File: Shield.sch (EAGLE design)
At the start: 1 part

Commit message: More to do listing
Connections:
- new net ESC_SIG1: B1.9
- new net ESC_SIG2: B1.10
- new net ESC_SIG3: B1.11
- new net ESC_SIG4: B1.6
- new net ESC_SIG5: B1.5
- new net ESC_SIG6: B1.3
- new net PWM1: B1.7
- new net PWM2: B1.8
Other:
- note added: "Capacitors (multiple sizes)"
- note added: "Don't forget labels :)"
- note added: "Optional flyback diodes"
- note added: "Power LEDs"
- note added: "Reverse voltage protection"
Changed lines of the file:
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@@
 <text x="43.18" y="83.82" size="1.778" layer="91">ESC solder bridges or header connections</text>
 <text x="182.88" y="22.86" size="1.778" layer="91">https://www.arduino.cc/en/uploads/Main/arduino-mega2560-schematic.pdf</text>
+<text x="15.24" y="93.98" size="1.778" layer="91">Capacitors (multiple sizes)</text>
+<text x="15.24" y="91.44" size="1.778" layer="91">Optional flyback diodes</text>
+<text x="33.02" y="170.18" size="1.778" layer="91">Reverse voltage protection</text>
+<text x="76.2" y="144.78" size="1.27" layer="91">Power LEDs</text>
+<text x="289.56" y="66.04" size="1.27" layer="91">Don't forget labels :)</text>
 </plain>
 <instances>
@@
 </segment>
 </net>
+<net name="ESC_SIG1" class="0">
+<segment>
+<pinref part="B1" gate="G$1" pin="9"/>
+<wire x1="203.2" y1="60.96" x2="200.66" y2="60.96" width="0.1524" layer="91"/>
+<label x="200.66" y="60.96" size="1.27" layer="95" rot="R180" xref="yes"/>
+</segment>
+</net>
+<net name="ESC_SIG2" class="0">
+<segment>
+<pinref part="B1" gate="G$1" pin="10"/>
+<wire x1="203.2" y1="58.42" x2="200.66" y2="58.42" width="0.1524" layer="91"/>
+<label x="200.66" y="58.42" size="1.27" layer="95" rot="R180" xref="yes"/>
+</segment>
+</net>
+<net name="ESC_SIG3" class="0">
+<segment>
+<pinref part="B1" gate="G$1" pin="11"/>
+<wire x1="203.2" y1="55.88" x2="200.66" y2="55.88" width="0.1524" layer="91"/>
+<label x="200.66" y="55.88" size="1.27" layer="95" rot="R180" xref="yes"/>
+</segment>
+</net>
+<net name="ESC_SIG4" class="0">
+<segment>
+<pinref part="B1" gate="G$1" pin="6"/>
+<wire x1="203.2" y1="68.58" x2="200.66" y2="68.58" width="0.1524" layer="91"/>
+<label x="200.66" y="68.58" size="1.27" layer="95" rot="R180" xref="yes"/>
+</segment>
+</net>
+<net name="ESC_SIG5" class="0">
+<segment>
+<pinref part="B1" gate="G$1" pin="5"/>
+<wire x1="203.2" y1="71.12" x2="200.66" y2="71.12" width="0.1524" layer="91"/>
+<label x="200.66" y="71.12" size="1.27" layer="95" rot="R180" xref="yes"/>
+</segment>
+</net>
+<net name="ESC_SIG6" class="0">
+<segment>
+<pinref part="B1" gate="G$1" pin="3"/>
+<wire x1="203.2" y1="76.2" x2="200.66" y2="76.2" width="0.1524" layer="91"/>
+<label x="200.66" y="76.2" size="1.27" layer="95" rot="R180" xref="yes"/>
+</segment>
+</net>
+<net name="PWM1" class="0">
+<segment>
+<pinref part="B1" gate="G$1" pin="7"/>
+<wire x1="203.2" y1="66.04" x2="200.66" y2="66.04" width="0.1524" layer="91"/>
+<label x="200.66" y="66.04" size="1.27" layer="95" rot="R180" xref="yes"/>
+</segment>
+</net>
+<net name="PWM2" class="0">
+<segment>
+<pinref part="B1" gate="G$1" pin="8"/>
+<wire x1="203.2" y1="63.5" x2="200.66" y2="63.5" width="0.1524" layer="91"/>
+<label x="200.66" y="63.5" size="1.27" layer="95" rot="R180" xref="yes"/>
+</segment>
+</net>

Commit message: Split into two sheets and add most existing parts
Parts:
- added C1: 1mF, SparkFun-Capacitors:1000UF-RADIAL-5MM-25V-20%
- added C2: 100uF, SparkFun-Capacitors:100UF-POLAR-RADIAL-2.5MM-25V-20%
- added D1, D2: (no value), SparkFun-LED:LED3MM
- added D3: (no value), diode:SCHOTTKY-DIODECB429-15
- added J1, J12, J13, J14, J15, J17, J18, J2: (no value), SparkFun-Connectors:CONN_02
- added J10, J11: (no value), Banana Plug PTH:BANANA_PTH
- added J16: (no value), SparkFun-Connectors:CONN_03-SCREW-5MM
- added J3, J4, J5: (no value), SparkFun-Connectors:CONN_03
- added J6: (no value), SparkFun-Connectors:CONN_04
- added J7, J8, J9: DF13-4P-1.25DSA, con-hirose-df13:DF13-4P-1.25DSA
- added JP1, JP2: JUMPER-SMT_2_NO_SILK, SparkFun-Jumpers:JUMPER-SMT_2_NO_SILK
- added Q1: 60V/32A/35mΩ, SparkFun-DiscreteSemi:MOSFET-NCH-FQP30N06L
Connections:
- new net 12V: D1.A, D3.A, J1.2, J10.1, J17.2, JP2.1, Q1.G
- new net 3V3: B1.3.3V, J6.4, J7.1, J8.1, J9.1
- new net GND_RAW: J11.1, Q1.D
- new net N$1: J16.3
- new net N$2: J13.1, JP1.1
- new net N$3: J13.2, JP1.2
- new net N$4: C1.+, C2.+, D3.C, JP2.2
- new net N$5: J16.2
- new net N$6: J16.1
- new net PWM3: B1.4, J5.3
- new net SCL: J6.3, J7.2, J8.2, J9.2
- new net SDA: J6.2, J7.3, J8.3, J9.3
- net 5V: now also D2.A, J12.2, J14.2, J15.2, J18.2, J2.2, J3.2, J4.2, J5.2
- net GND: now also C1.-, C2.-, D1.C, D2.C, J1.1, J12.1, J14.1, J15.1, J17.1, J18.1, J2.1, J3.1, J4.1, J5.1, J6.1, J7.4, J8.4, J9.4, Q1.S
- net PWM1: now also J3.3
- net PWM2: now also J4.3
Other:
- note added: "5 mm screw terminal connector"
- note added: "5V outputs (and usb)"
- note added: "Fuses"
- note added: "I2C Breakout & Connectors"
- note added: "Mounting holes"
- note added: "Multiple size capacitors. Pick the value to your application"
- note added: "Optional schottky diode for back emf protection"
- note added: "PWM Connectors"
- note added: "Solder jumper / header jumper for connecting & disconnecting PWM signal"
- note added: "Voltage Testpoints and power indicator LEDs"
- note removed: "5V outputs"
- note removed: "Capacitors (multiple sizes)"
- note removed: "ESC connections"
- note removed: "ESC solder bridges or header connections"
- note removed: "I2C breakouts"
- note removed: "Optional flyback diodes"
- note removed: "Power LEDs"
- note removed: "Servo headers"

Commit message: Finish all parts except fuses
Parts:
- added C10, C12, C4, C6, C8: 100uF, SparkFun-Capacitors:100UF-POLAR-RADIAL-2.5MM-25V-20%
- added C11, C3, C5, C7, C9: 1mF, SparkFun-Capacitors:1000UF-RADIAL-5MM-25V-20%
- added D4, D5, D6, D7, D8: (no value), diode:SCHOTTKY-DIODECB429-15
- added H1, H2, H3, H4, H5, H6: 6-32-HOLE, Mounting Holes:6-32-HOLE
- added J19, J21, J23, J25, J27: (no value), SparkFun-Connectors:CONN_02
- added J20, J22, J24, J26, J28: (no value), SparkFun-Connectors:CONN_03-SCREW-5MM
- added J29: (no value), SparkFun-Connectors:CONN_03
- added J30: (no value), Anderson PP:ANDERON_POWERPOLE_2
- added JP10, JP11, JP12, JP13, JP14, JP15, JP16, JP3, JP4, JP5, JP6, JP7, JP8, JP9: JUMPER-SMT_2_NO_SILK, SparkFun-Jumpers:JUMPER-SMT_2_NO_SILK
- added R1, R2: 10k, SparkFun-Resistors:10KOHM-HORIZ-1/4W-5%
- added U$1, U$2, U$3, U$4, U$5, U$6: ESC, ESC:ESC
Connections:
- removed net N$1: J16.3
- removed net N$2: J13.1, JP1.1
- removed net N$3: J13.2, JP1.2
- removed net N$4: C1.+, C2.+, D3.C, JP2.2
- removed net N$5: J16.2
- removed net N$6: J16.1
- new net 12V_ESC1: C1.+, C2.+, D3.C, JP2.2, U$1.VCC
- new net 12V_ESC2: C3.+, C4.+, D4.C, JP8.2, U$2.VCC
- new net 12V_ESC3: C5.+, C6.+, D5.C, JP10.2, U$3.VCC
- new net 12V_ESC4: C7.+, C8.+, D6.C, JP12.2, U$4.VCC
- new net 12V_ESC5: C10.+, C9.+, D7.C, JP14.2, U$5.VCC
- new net 12V_ESC6: C11.+, C12.+, D8.C, JP16.2, U$6.VCC
- new net ESC1_PH1: J16.3, U$1.RED
- new net ESC1_PH2: J16.2, U$1.YEL
- new net ESC1_PH3: J16.1, U$1.BLK
- new net ESC2_PH1: J20.3, U$2.RED
- new net ESC2_PH2: J20.2, U$2.YEL
- new net ESC2_PH3: J20.1, U$2.BLK
- new net ESC3_PH1: J22.3, U$3.RED
- new net ESC3_PH2: J22.2, U$3.YEL
- new net ESC3_PH3: J22.1, U$3.BLK
- new net ESC4_PH1: J24.3, U$4.RED
- new net ESC4_PH2: J24.2, U$4.YEL
- new net ESC4_PH3: J24.1, U$4.BLK
- new net ESC5_PH1: J26.3, U$5.RED
- new net ESC5_PH2: J26.2, U$5.YEL
- new net ESC5_PH3: J26.1, U$5.BLK
- new net ESC6_PH1: J28.3, U$6.RED
- new net ESC6_PH2: J28.2, U$6.YEL
- new net ESC6_PH3: J28.1, U$6.BLK
- new net ESC_SIG_PIN1: J13.2, JP1.2, U$1.PWM_SGN
- new net ESC_SIG_PIN2: J19.2, JP7.2, U$2.PWM_SGN
- new net ESC_SIG_PIN3: J21.2, JP9.2, U$3.PWM_SGN
- new net ESC_SIG_PIN4: J23.2, JP11.2, U$4.PWM_SGN
- new net ESC_SIG_PIN5: J25.2, JP13.2, U$5.PWM_SGN
- new net ESC_SIG_PIN6: J27.2, JP15.2, U$6.PWM_SGN
- new net N$10: B1.A5, JP4.2
- new net N$7: JP5.1, JP6.1, R1.2, R2.2
- new net N$9: B1.A4, JP3.2
- net 12V: now also D4.A, D5.A, D6.A, D7.A, D8.A, J29.3, J30.POS, JP10.1, JP12.1, JP14.1, JP16.1, JP8.1
- net 3V3: now also JP5.2
- net 5V: now also J29.1, JP6.2
- net ESC_SIG1: now also J13.1, JP1.1
- net ESC_SIG2: now also J19.1, JP7.1
- net ESC_SIG3: now also J21.1, JP9.1
- net ESC_SIG4: now also J23.1, JP11.1
- net ESC_SIG5: now also J25.1, JP13.1
- net ESC_SIG6: now also J27.1, JP15.1
- net GND: now also C10.-, C11.-, C12.-, C3.-, C4.-, C5.-, C6.-, C7.-, C8.-, C9.-, J29.2, U$1.GND, U$1.PWM_GND, U$2.GND, U$2.PWM_GND, U$3.GND, U$3.PWM_GND, U$4.GND, U$4.PWM_GND, U$5.GND, U$5.PWM_GND, U$6.GND, U$6.PWM_GND
- net GND_RAW: now also J30.NEG
- net SCL: now also B1.21(SCL), JP4.1, R1.1
- net SDA: now also B1.20(SDA), JP3.1, R2.1
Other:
- note added: "12->5V converter Use a board mount power supply like CUI P78E-1000 or recom INNOLINE R-78E. Or connect and external one with wires"
- note added: "5V outputs"
- note added: "Populate eiter JP5 or JP6 (not both) for I2C logic level"
- note added: "https://www.arduino.cc/en/uploads/Main/arduino-uno-schematic.pdf https://www.arduino.cc/en/uploads/Main/arduino-mega2560-schematic.pdf"
- note removed: "12->5V converter"
- note removed: "5V outputs (and usb)"
- note removed: "6x ESCs"
- note removed: "https://www.arduino.cc/en/uploads/Main/arduino-mega2560-schematic.pdf"
- moved on the sheet: C1, C2, D3, J12, J13, J14, J15, J16, JP1, JP2

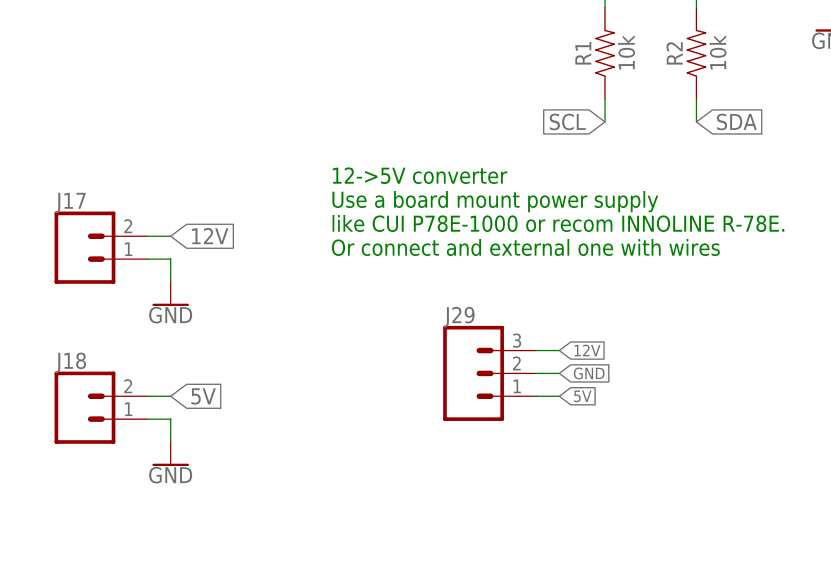
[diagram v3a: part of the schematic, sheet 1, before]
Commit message: Add caps around buck converter (fixes #1)
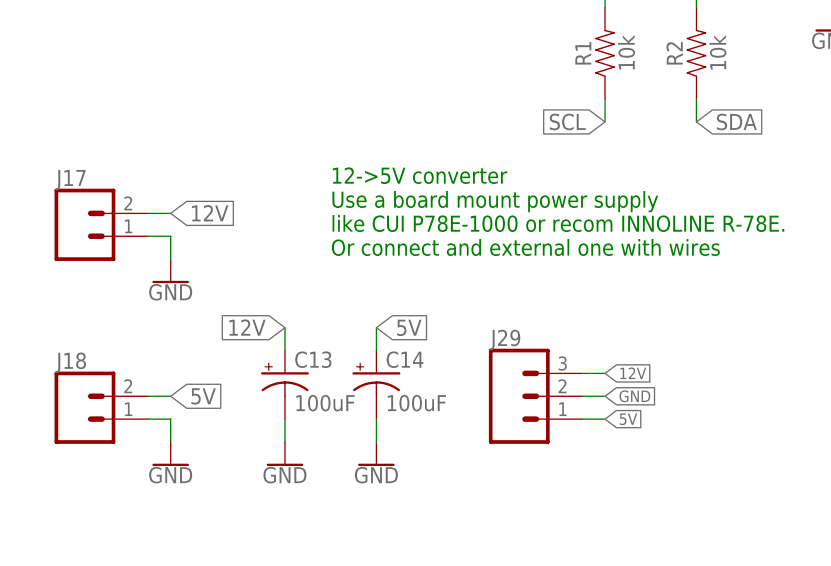
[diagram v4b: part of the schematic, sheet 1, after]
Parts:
- added C13, C14: 100uF, SparkFun-Capacitors:100UF-POLAR-RADIAL-2.5MM-25V-20%
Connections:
- net 12V: now also C13.+
- net 5V: now also C14.+
- net GND: now also C13.-, C14.-
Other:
- moved on the sheet: J17, J29
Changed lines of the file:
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@@
 <part name="J29" library="SparkFun-Connectors" library_urn="urn:adsk.eagle:library:513" deviceset="CONN_03" device="" package3d_urn="urn:adsk.eagle:package:38063/1"/>
 <part name="J30" library="Anderson PP" deviceset="ANDERON_POWERPOLE_2" device=""/>
+<part name="C13" library="SparkFun-Capacitors" library_urn="urn:adsk.eagle:library:510" deviceset="100UF-POLAR" device="-RADIAL-2.5MM-25V-20%" package3d_urn="urn:adsk.eagle:package:37415/1" value="100uF"/>
+<part name="C14" library="SparkFun-Capacitors" library_urn="urn:adsk.eagle:library:510" deviceset="100UF-POLAR" device="-RADIAL-2.5MM-25V-20%" package3d_urn="urn:adsk.eagle:package:37415/1" value="100uF"/>
+<part name="GND31" library="SparkFun-PowerSymbols" library_urn="urn:adsk.eagle:library:530" deviceset="GND" device=""/>
+<part name="GND32" library="SparkFun-PowerSymbols" library_urn="urn:adsk.eagle:library:530" deviceset="GND" device=""/>
 </parts>
 <sheets>
@@
 <attribute name="VALUE" x="33.02" y="68.326" size="1.778" layer="96" align="top-center"/>
 </instance>
-<instance part="J17" gate="G$1" x="7.62" y="33.02" smashed="yes">
-<attribute name="VALUE" x="5.08" y="28.194" size="1.778" layer="96" font="vector"/>
-<attribute name="NAME" x="5.08" y="38.608" size="1.778" layer="95" font="vector"/>
+<instance part="J17" gate="G$1" x="7.62" y="35.56" smashed="yes">
+<attribute name="VALUE" x="5.08" y="30.734" size="1.778" layer="96" font="vector"/>
+<attribute name="NAME" x="5.08" y="41.148" size="1.778" layer="95" font="vector"/>
 </instance>
 <instance part="J18" gate="G$1" x="7.62" y="15.24" smashed="yes">
@@
 <attribute name="NAME" x="5.08" y="20.828" size="1.778" layer="95" font="vector"/>
 </instance>
-<instance part="GND18" gate="1" x="17.78" y="27.94" smashed="yes">
-<attribute name="VALUE" x="17.78" y="27.686" size="1.778" layer="96" align="top-center"/>
+<instance part="GND18" gate="1" x="17.78" y="30.48" smashed="yes">
+<attribute name="VALUE" x="17.78" y="30.226" size="1.778" layer="96" align="top-center"/>
 </instance>
 <instance part="GND19" gate="1" x="17.78" y="10.16" smashed="yes">
@@
 <attribute name="VALUE" x="170.18" y="2.54" size="1.016" layer="95" align="top-center"/>
 </instance>
-<instance part="J29" gate="J$1" x="50.8" y="20.32" smashed="yes">
-<attribute name="VALUE" x="48.26" y="12.954" size="1.778" layer="96" font="vector"/>
-<attribute name="NAME" x="48.26" y="25.908" size="1.778" layer="95" font="vector"/>
+<instance part="J29" gate="J$1" x="55.88" y="17.78" smashed="yes">
+<attribute name="VALUE" x="53.34" y="10.414" size="1.778" layer="96" font="vector"/>
+<attribute name="NAME" x="53.34" y="23.368" size="1.778" layer="95" font="vector"/>
 </instance>
 <instance part="J30" gate="G$1" x="7.62" y="152.4" smashed="yes">
 <attribute name="NAME" x="5.08" y="155.448" size="1.778" layer="95" font="vector"/>
+</instance>
+<instance part="C13" gate="G$1" x="30.48" y="20.32" smashed="yes">
+<attribute name="NAME" x="31.496" y="20.955" size="1.778" layer="95" font="vector"/>
+<attribute name="VALUE" x="31.496" y="16.129" size="1.778" layer="96" font="vector"/>
+</instance>
+<instance part="C14" gate="G$1" x="40.64" y="20.32" smashed="yes">
+<attribute name="NAME" x="41.656" y="20.955" size="1.778" layer="95" font="vector"/>
+<attribute name="VALUE" x="41.656" y="16.129" size="1.778" layer="96" font="vector"/>
+</instance>
+<instance part="GND31" gate="1" x="30.48" y="10.16" smashed="yes">
+<attribute name="VALUE" x="30.48" y="9.906" size="1.778" layer="96" align="top-center"/>
+</instance>
+<instance part="GND32" gate="1" x="40.64" y="10.16" smashed="yes">
+<attribute name="VALUE" x="40.64" y="9.906" size="1.778" layer="96" align="top-center"/>
 </instance>
 </instances>
@@
 <segment>
 <pinref part="J17" gate="G$1" pin="1"/>
-<wire x1="15.24" y1="33.02" x2="17.78" y2="33.02" width="0.1524" layer="91"/>
+<wire x1="15.24" y1="35.56" x2="17.78" y2="35.56" width="0.1524" layer="91"/>
 <pinref part="GND18" gate="1" pin="GND"/>
-<wire x1="17.78" y1="33.02" x2="17.78" y2="30.48" width="0.1524" layer="91"/>
+<wire x1="17.78" y1="35.56" x2="17.78" y2="33.02" width="0.1524" layer="91"/>
 </segment>
 <segment>
 <pinref part="J29" gate="J$1" pin="2"/>
-<wire x1="58.42" y1="20.32" x2="60.96" y2="20.32" width="0.1524" layer="91"/>
-<label x="60.96" y="20.32" size="1.27" layer="95" xref="yes"/>
+<wire x1="63.5" y1="17.78" x2="66.04" y2="17.78" width="0.1524" layer="91"/>
+<label x="66.04" y="17.78" size="1.27" layer="95" xref="yes"/>
+</segment>
+<segment>
+<pinref part="C13" gate="G$1" pin="-"/>
+<pinref part="GND31" gate="1" pin="GND"/>
+<wire x1="30.48" y1="15.24" x2="30.48" y2="12.7" width="0.1524" layer="91"/>
+</segment>
+<segment>
+<pinref part="GND32" gate="1" pin="GND"/>
+<pinref part="C14" gate="G$1" pin="-"/>
+<wire x1="40.64" y1="12.7" x2="40.64" y2="15.24" width="0.1524" layer="91"/>
 </segment>
 </net>
@@
 <segment>
 <pinref part="J29" gate="J$1" pin="1"/>
-<wire x1="58.42" y1="17.78" x2="60.96" y2="17.78" width="0.1524" layer="91"/>
-<label x="60.96" y="17.78" size="1.27" layer="95" xref="yes"/>
+<wire x1="63.5" y1="15.24" x2="66.04" y2="15.24" width="0.1524" layer="91"/>
+<label x="66.04" y="15.24" size="1.27" layer="95" xref="yes"/>
+</segment>
+<segment>
+<pinref part="C14" gate="G$1" pin="+"/>
+<wire x1="40.64" y1="22.86" x2="40.64" y2="25.4" width="0.1524" layer="91"/>
+<label x="40.64" y="25.4" size="1.778" layer="95" xref="yes"/>
 </segment>
 </net>
@@
 <segment>
 <pinref part="J17" gate="G$1" pin="2"/>
-<wire x1="15.24" y1="35.56" x2="17.78" y2="35.56" width="0.1524" layer="91"/>
-<label x="17.78" y="35.56" size="1.778" layer="95" xref="yes"/>
+<wire x1="15.24" y1="38.1" x2="17.78" y2="38.1" width="0.1524" layer="91"/>
+<label x="17.78" y="38.1" size="1.778" layer="95" xref="yes"/>
 </segment>
 <segment>
 <pinref part="J29" gate="J$1" pin="3"/>
-<wire x1="58.42" y1="22.86" x2="60.96" y2="22.86" width="0.1524" layer="91"/>
-<label x="60.96" y="22.86" size="1.27" layer="95" xref="yes"/>
+<wire x1="63.5" y1="20.32" x2="66.04" y2="20.32" width="0.1524" layer="91"/>
+<label x="66.04" y="20.32" size="1.27" layer="95" xref="yes"/>
 </segment>
 <segment>
@@
 <label x="20.32" y="152.4" size="1.27" layer="95" xref="yes"/>
 </segment>
-</net>
+<segment>
+<pinref part="C13" gate="G$1" pin="+"/>
+<wire x1="30.48" y1="22.86" x2="30.48" y2="25.4" width="0.1524" layer="91"/>
+<label x="30.48" y="25.4" size="1.778" layer="95" rot="R180" xref="yes"/>
+</segment>
+</net>

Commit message: Size ESC for 0.1" gnd & sig headers. Add and use expansion.
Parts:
- added J31, J32: ESC_EXPANSION_CONNECTOR, Esc Expansion:ESC_EXPANSION_CONNECTOR
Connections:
- new net ESC_SIG_EXP_PIN4: J32.SIG1, U$4.PWM_SGN
- new net ESC_SIG_EXP_PIN5: J32.SIG2, U$5.PWM_SGN
- new net ESC_SIG_EXP_PIN6: J32.SIG3, U$6.PWM_SGN
- net 12V: now also J31.VCC, J32.VCC
- net ESC1_PH1: now also U$1.WHT; no longer U$1.RED
- net ESC1_PH2: now also U$1.GRN; no longer U$1.YEL
- net ESC1_PH3: now also U$1.BLUE; no longer U$1.BLK
- net ESC2_PH1: now also U$2.WHT; no longer U$2.RED
- net ESC2_PH2: now also U$2.GRN; no longer U$2.YEL
- net ESC2_PH3: now also U$2.BLUE; no longer U$2.BLK
- net ESC3_PH1: now also U$3.WHT; no longer U$3.RED
- net ESC3_PH2: now also U$3.GRN; no longer U$3.YEL
- net ESC3_PH3: now also U$3.BLUE; no longer U$3.BLK
- net ESC4_PH1: now also U$4.WHT; no longer U$4.RED
- net ESC4_PH2: now also U$4.GRN; no longer U$4.YEL
- net ESC4_PH3: now also U$4.BLUE; no longer U$4.BLK
- net ESC5_PH1: now also U$5.WHT; no longer U$5.RED
- net ESC5_PH2: now also U$5.GRN; no longer U$5.YEL
- net ESC5_PH3: now also U$5.BLUE; no longer U$5.BLK
- net ESC6_PH1: now also U$6.WHT; no longer U$6.RED
- net ESC6_PH2: now also U$6.GRN; no longer U$6.YEL
- net ESC6_PH3: now also U$6.BLUE; no longer U$6.BLK
- net ESC_SIG_PIN4: now also J31.SIG1; no longer U$4.PWM_SGN
- net ESC_SIG_PIN5: now also J31.SIG2; no longer U$5.PWM_SGN
- net ESC_SIG_PIN6: now also J31.SIG3; no longer U$6.PWM_SGN
- net GND: now also J31.GND, J32.GND
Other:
- moved on the sheet: D1

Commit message: Begin board placement
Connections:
- net N$10 renamed A5_SCL
- net N$7 renamed I2C_VCC
- net N$9 renamed A4_SDA
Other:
- note added: "Don't forget labels :) LIGHTS?"
- note added: "NEED NEW REVISION CONNECTOR FOR I2C?"
- note added: "NEED NEW REVISION CONNECTOR? DOUBLE CHECK PINOUT ISN'T MIRRORED"
- note removed: "Don't forget labels :)"
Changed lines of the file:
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@@
 <text x="81.28" y="170.18" size="1.778" layer="91">Reverse voltage protection</text>
 <text x="129.54" y="160.02" size="1.778" layer="91">Voltage Testpoints and power indicator LEDs</text>
-<text x="289.56" y="66.04" size="1.27" layer="91">Don't forget labels :)</text>
+<text x="289.56" y="66.04" size="5.08" layer="91">Don't forget labels :)
+LIGHTS?</text>
 <text x="116.84" y="81.28" size="1.778" layer="91">I2C Breakout &amp; Connectors</text>
 <text x="127" y="38.1" size="1.778" layer="91">PWM Connectors</text>
@@
 <text x="60.96" y="101.6" size="1.778" layer="91" align="top-left">Populate eiter JP5 or JP6 (not both)
 for I2C logic level</text>
+<text x="106.68" y="86.36" size="1.778" layer="91">NEED NEW REVISION CONNECTOR?
+DOUBLE CHECK PINOUT ISN'T MIRRORED</text>
+<text x="55.88" y="-38.1" size="5.08" layer="91">NEED NEW REVISION CONNECTOR FOR I2C?</text>
 </plain>
 <instances>
@@
 </segment>
 </net>
-<net name="N$9" class="0">
+<net name="A4_SDA" class="0">
 <segment>
 <pinref part="B1" gate="G$1" pin="A4"/>
@@
 </segment>
 </net>
-<net name="N$10" class="0">
+<net name="A5_SCL" class="0">
 <segment>
 <pinref part="B1" gate="G$1" pin="A5"/>
@@
 </segment>
 </net>
-<net name="N$7" class="0">
+<net name="I2C_VCC" class="0">
 <segment>
 <pinref part="R1" gate="G$1" pin="2"/>
@@
 <wire x1="76.2" y1="63.5" x2="78.74" y2="63.5" width="0.1524" layer="91"/>
 <junction x="76.2" y="63.5"/>
-</segment>
-</net>
+<label x="66.04" y="63.5" size="1.778" layer="95"/>
+</segment>
+</net>
